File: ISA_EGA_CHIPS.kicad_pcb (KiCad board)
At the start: 2 copper layers, 131.1 x 108 mm, 67 parts, among them J1 EGA Feature Connector, J2 Light Pen, J3 RCA 1, J4 RCA 2, J6 Digital Output, J7 Bus_ISA_8bit, SW1 Configuration, U1 41464, U10 27C256, U11 82A436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

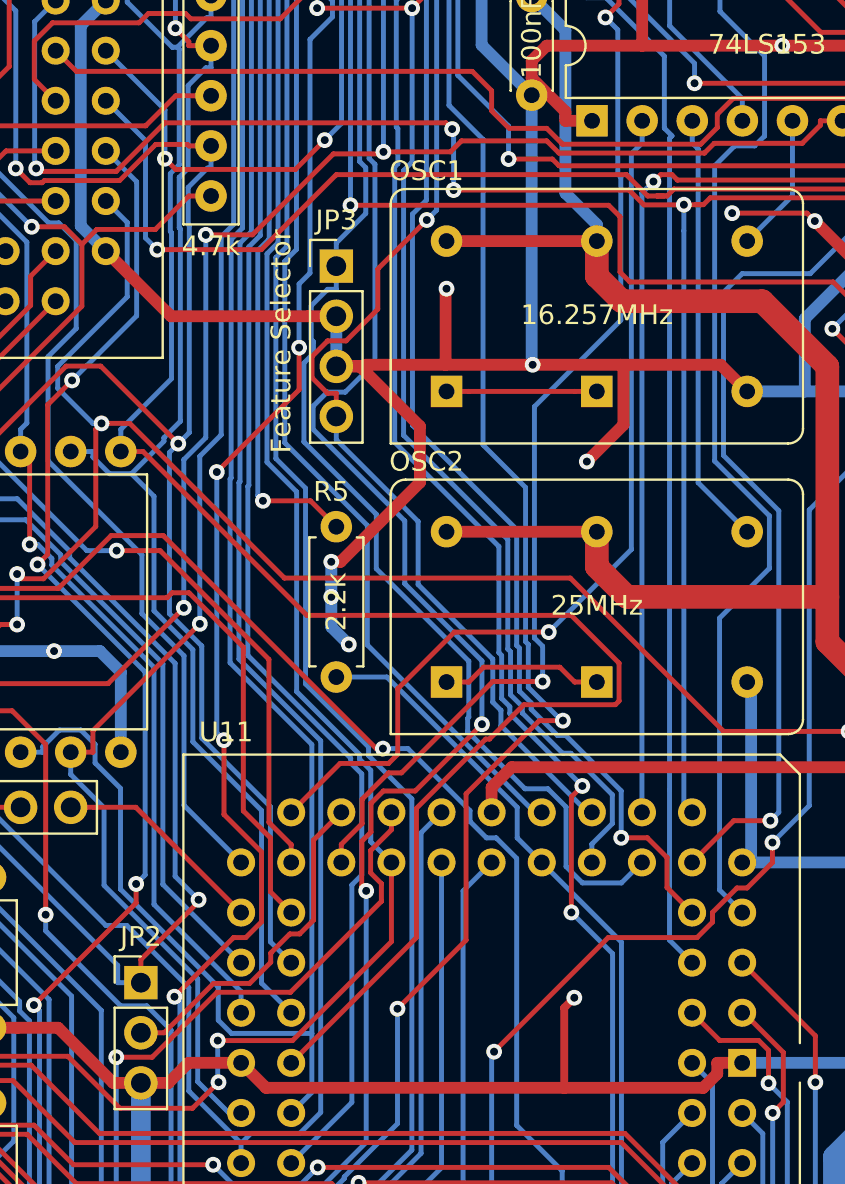
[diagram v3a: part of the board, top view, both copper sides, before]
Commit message: Add some more grounding
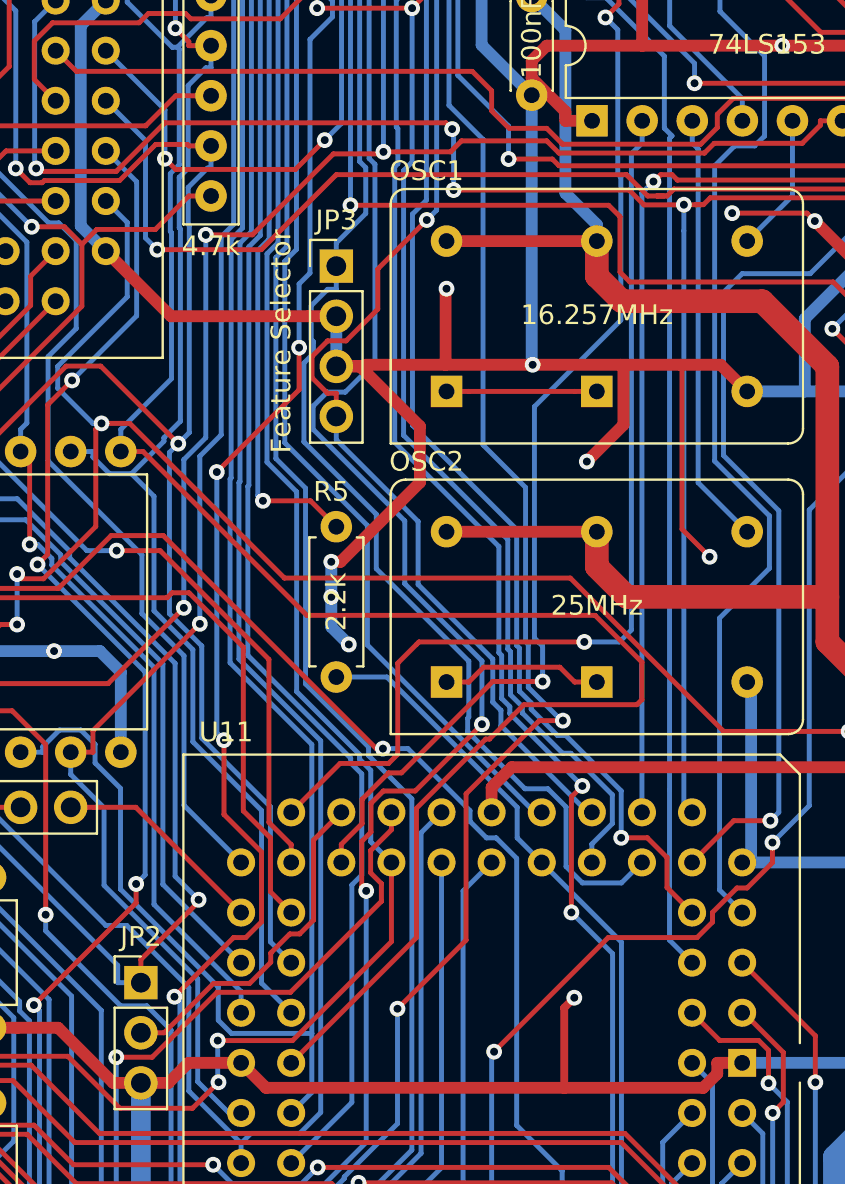
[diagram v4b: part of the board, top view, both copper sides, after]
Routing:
- net GND: track 1026.4 -> 1036.8 mm, vias 16 -> 17
- net /CLKSEL1: track 46.7 -> 49.8 mm
- net /BUF_D3: track 111.8 -> 114.1 mm
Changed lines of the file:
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@@
     (thickness 1.6)
     (drawings 22)
-    (tracks 4120)
+    (tracks 4128)
     (zones 0)
     (modules 67)
@@
   (via (at 273.05 144.272) (size 0.8) (drill 0.4) (layers F.Cu B.Cu) (net 1))
   (segment (start 274.7476 139.3656) (end 274.908001 139.526001) (width 0.6) (layer F.Cu) (net 1))
-  (segment (start 279.8276 139.3656) (end 274.7476 139.3656) (width 0.6) (layer F.Cu) (net 1))
   (segment (start 274.7476 139.3656) (end 270.3026 139.3656) (width 0.6) (layer F.Cu) (net 1))
   (via (at 221.488 152.527) (size 0.8) (drill 0.4) (layers F.Cu B.Cu) (net 1))
@@
   (segment (start 284.205711 131.678711) (end 280.416 131.678711) (width 0.25) (layer F.Cu) (net 1))
   (segment (start 284.607 132.08) (end 284.205711 131.678711) (width 0.25) (layer F.Cu) (net 1))
+  (via (at 279.273 149.098) (size 0.8) (drill 0.4) (layers F.Cu B.Cu) (net 1))
+  (segment (start 279.273 149.098) (end 277.876 147.701) (width 0.25) (layer F.Cu) (net 1))
+  (segment (start 277.876 147.701) (end 277.876 139.446) (width 0.25) (layer F.Cu) (net 1))
+  (segment (start 277.7956 139.3656) (end 274.7476 139.3656) (width 0.6) (layer F.Cu) (net 1))
+  (segment (start 277.876 139.446) (end 277.7956 139.3656) (width 0.25) (layer F.Cu) (net 1))
+  (segment (start 279.8276 139.3656) (end 277.7956 139.3656) (width 0.6) (layer F.Cu) (net 1))
   (segment (start 297.3537 109.22) (end 297.2594 109.3143) (width 0.6) (layer F.Cu) (net 2))
   (segment (start 297.2594 109.3143) (end 287.7666 109.3143) (width 0.6) (layer F.Cu) (net 2))
@@
   (segment (start 252.8747 122.9848) (end 252.8747 123.19) (width 0.25) (layer F.Cu) (net 99))
   (via (at 252.1961 122.3062) (size 0.8) (layers F.Cu B.Cu) (net 99))
-  (segment (start 249.428 143.764) (end 250.5533 143.764) (width 0.25) (layer F.Cu) (net 100))
-  (segment (start 250.5533 143.764) (end 258.8581 152.0688) (width 0.25) (layer F.Cu) (net 100))
-  (segment (start 258.8581 152.0688) (end 272.2634 152.0688) (width 0.25) (layer F.Cu) (net 100))
-  (segment (start 272.2634 152.0688) (end 274.6834 154.4888) (width 0.25) (layer F.Cu) (net 100))
-  (segment (start 274.6834 154.4888) (end 274.6834 156.4097) (width 0.25) (layer F.Cu) (net 100))
-  (segment (start 274.6834 156.4097) (end 274.4964 156.5967) (width 0.25) (layer F.Cu) (net 100))
-  (segment (start 274.4964 156.5967) (end 269.8583 156.5967) (width 0.25) (layer F.Cu) (net 100))
-  (segment (start 269.8583 156.5967) (end 268.1172 158.3378) (width 0.25) (layer F.Cu) (net 100))
-  (segment (start 268.1172 158.3378) (end 267.9234 158.3378) (width 0.25) (layer F.Cu) (net 100))
-  (segment (start 267.9234 158.3378) (end 264.414 161.8472) (width 0.25) (layer F.Cu) (net 100))
-  (segment (start 264.414 161.8472) (end 264.414 168.402) (width 0.25) (layer F.Cu) (net 100))
-  (segment (start 264.414 168.402) (end 258.064 174.752) (width 0.25) (layer F.Cu) (net 100))
   (segment (start 249.428 142.6387) (end 251.9967 140.07) (width 0.25) (layer B.Cu) (net 100))
   (segment (start 251.9967 140.07) (end 251.9967 132.6675) (width 0.25) (layer B.Cu) (net 100))
@@
   (segment (start 249.428 143.764) (end 249.428 142.6387) (width 0.25) (layer B.Cu) (net 100))
   (segment (start 254 120.65) (end 254 121.7753) (width 0.25) (layer B.Cu) (net 100))
+  (segment (start 273.46929 152.0688) (end 258.8581 152.0688) (width 0.25) (layer F.Cu) (net 100))
+  (segment (start 258.8581 152.0688) (end 250.5533 143.764) (width 0.25) (layer F.Cu) (net 100))
+  (segment (start 269.8583 156.5967) (end 275.5843 156.5967) (width 0.25) (layer F.Cu) (net 100))
+  (segment (start 268.1172 158.3378) (end 269.8583 156.5967) (width 0.25) (layer F.Cu) (net 100))
+  (segment (start 267.9234 158.3378) (end 268.1172 158.3378) (width 0.25) (layer F.Cu) (net 100))
+  (segment (start 275.844 154.44351) (end 273.46929 152.0688) (width 0.25) (layer F.Cu) (net 100))
+  (segment (start 275.844 156.337) (end 275.844 154.44351) (width 0.25) (layer F.Cu) (net 100))
+  (segment (start 275.5843 156.5967) (end 275.844 156.337) (width 0.25) (layer F.Cu) (net 100))
+  (segment (start 264.414 161.8472) (end 267.9234 158.3378) (width 0.25) (layer F.Cu) (net 100))
+  (segment (start 250.5533 143.764) (end 249.428 143.764) (width 0.25) (layer F.Cu) (net 100))
+  (segment (start 264.414 168.402) (end 264.414 161.8472) (width 0.25) (layer F.Cu) (net 100))
+  (segment (start 258.064 174.752) (end 264.414 168.402) (width 0.25) (layer F.Cu) (net 100))
   (segment (start 253.4322 152.4974) (end 253.4322 144.0007) (width 0.25) (layer B.Cu) (net 101))
   (segment (start 253.4322 144.0007) (end 254.5152 142.9177) (width 0.25) (layer B.Cu) (net 101))
@@
   (segment (start 274.6195 122.3851) (end 274.6195 129.7008) (width 0.25) (layer B.Cu) (net 156))
   (segment (start 273.9925 121.7581) (end 274.6195 122.3851) (width 0.25) (layer B.Cu) (net 156))
-  (segment (start 275.854 127) (end 275.854 128.1253) (width 0.25) (layer B.Cu) (net 157))
-  (segment (start 271.1194 152.9156) (end 266.3371 152.9156) (width 0.25) (layer F.Cu) (net 157))
-  (segment (start 266.3371 152.9156) (end 263.465 155.7877) (width 0.25) (layer F.Cu) (net 157))
   (segment (start 263.465 155.7877) (end 263.465 159.1095) (width 0.25) (layer F.Cu) (net 157))
   (segment (start 263.465 159.1095) (end 262.9987 159.5758) (width 0.25) (layer F.Cu) (net 157))
   (segment (start 262.9987 159.5758) (end 260.5402 159.5758) (width 0.25) (layer F.Cu) (net 157))
   (segment (start 260.5402 159.5758) (end 258.064 162.052) (width 0.25) (layer F.Cu) (net 157))
-  (segment (start 275.854 128.1253) (end 275.3086 128.6707) (width 0.25) (layer B.Cu) (net 157))
-  (segment (start 275.3086 128.6707) (end 275.3086 148.7264) (width 0.25) (layer B.Cu) (net 157))
-  (segment (start 275.3086 148.7264) (end 271.1194 152.9156) (width 0.25) (layer B.Cu) (net 157))
-  (via (at 271.1194 152.9156) (size 0.8) (layers F.Cu B.Cu) (net 157))
+  (segment (start 263.465 155.7877) (end 263.465 154.492) (width 0.25) (layer F.Cu) (net 157))
+  (segment (start 263.465 154.492) (end 264.414 153.543) (width 0.25) (layer F.Cu) (net 157))
+  (via (at 272.923 153.416) (size 0.8) (drill 0.4) (layers F.Cu B.Cu) (net 157))
+  (segment (start 264.541 153.416) (end 272.923 153.416) (width 0.25) (layer F.Cu) (net 157))
+  (segment (start 264.414 153.543) (end 264.541 153.416) (width 0.25) (layer F.Cu) (net 157))
+  (segment (start 275.854 128.1253) (end 275.854 127) (width 0.25) (layer B.Cu) (net 157))
+  (segment (start 275.3086 128.6707) (end 275.854 128.1253) (width 0.25) (layer B.Cu) (net 157))
+  (segment (start 275.3086 152.8084) (end 275.3086 128.6707) (width 0.25) (layer B.Cu) (net 157))
+  (segment (start 274.701 153.416) (end 275.3086 152.8084) (width 0.25) (layer B.Cu) (net 157))
+  (segment (start 272.923 153.416) (end 274.701 153.416) (width 0.25) (layer B.Cu) (net 157))
   (segment (start 278.384 164.592) (end 280.5001 162.4759) (width 0.25) (layer F.Cu) (net 158))
   (segment (start 280.5001 162.4759) (end 282.3568 162.4759) (width 0.25) (layer F.Cu) (net 158))
